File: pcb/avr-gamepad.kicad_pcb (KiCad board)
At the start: 2 copper layers, 53.1 x 53 mm, 57 parts, among them J1 Conn_01x06, J2 Conn_01x06, J3 Conn_01x05, J4 Conn_01x05, P1 USB_C_Plug_USB2.0, SW1 RESET, SW10 R2, SW11 A, SW13 Left, SW14 L2, SW16 B, SW17 Start, SW18 Y, SW19 X, SW2 Right, SW3 Up, SW4 Down, SW6 Select, SW7 L1, SW8 R1, U1 ATmega32U4-AU, U2 PCF8574, U3 PCF8574, Y1 Crystal_GND24

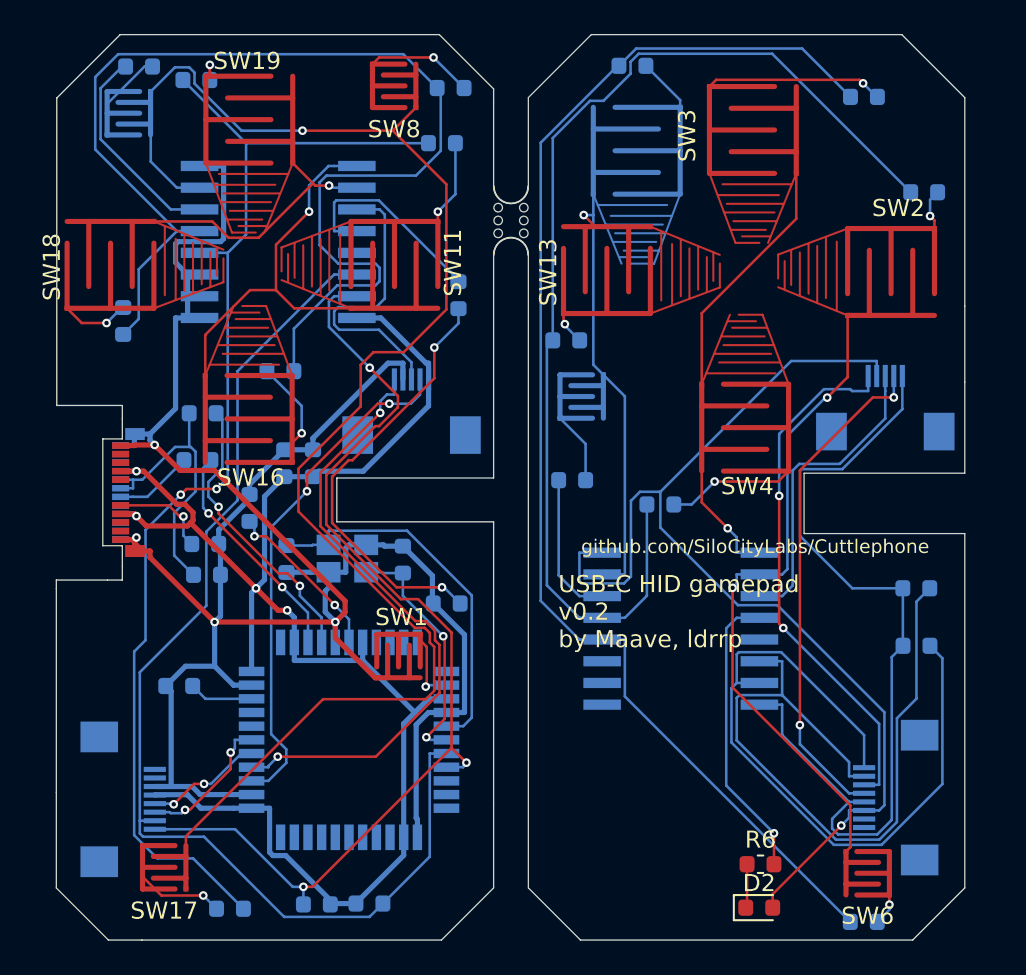
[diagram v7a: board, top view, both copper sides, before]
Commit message: pcb rearranging, placeholder footprint for right angle tact switches
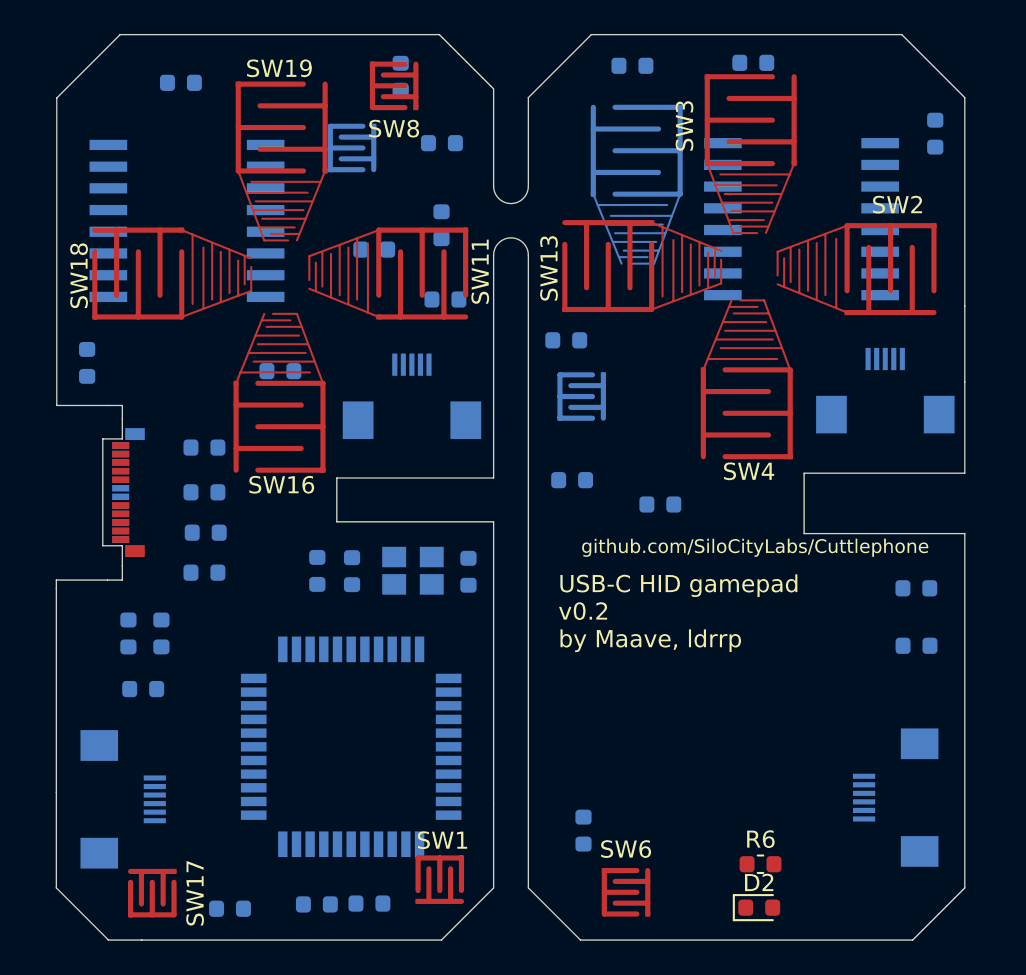
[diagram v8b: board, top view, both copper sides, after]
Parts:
- removed mouse-bite-2mm-slot: VAL**, Panelization:mouse-bite-2mm-slot
- J1, J2: footprint Connector_FFC-FPC:Hirose_FH12-8S-0.5SH_1x08-1MP_P0.50mm_Horizontal -> Connector_FFC-FPC:Hirose_FH12-6S-0.5SH_1x06-1MP_P0.50mm_Horizontal
- moved U2 25.0 mm to (171.0, 91.2)
- moved D1 17.8 mm to (150.2, 95.9)
- moved D13 17.4 mm to (146.0, 93.0), turned to 180 degrees
- moved D3 17.2 mm to (158.3, 126.9), turned to 270 degrees
- moved SW6 14.2 mm to (160.8, 130.6), turned to 0 degrees
- moved C1 13.5 mm to (131.7, 115.4)
- moved C2 13.3 mm to (133.6, 115.4)
- moved SW1 13.3 mm to (149.9, 129.8)
- moved SW10 13.2 mm to (144.8, 87.0)
- moved R4 7.44 mm to (136.1, 104.5)
- moved D8 6.77 mm to (168.2, 82.0)
- moved U3 5.47 mm to (135.1, 91.3)
- moved C6 5.41 mm to (142.7, 111.8)
- moved R1 4.62 mm to (136.1, 107.2)
- moved R2 4.27 mm to (136.2, 109.5)
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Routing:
- net GND: track 142.1 -> 0.00 mm, vias 4 -> 0
- net +5V: track 93.5 -> 0.00 mm, vias 4 -> 0
- net /Col1: track 89.6 -> 0.00 mm, vias 1 -> 0
- net /RowL1: track 76.2 -> 0.00 mm
- net /Row1: track 69.9 -> 0.00 mm, vias 2 -> 0
- net /Row2: track 69.8 -> 0.00 mm
- net /SCL: track 67.1 -> 0.00 mm
- net /RowL2: track 65.6 -> 0.00 mm
- net /GND_L: track 64.1 -> 0.00 mm, vias 1 -> 0
- net /SDA: track 60.7 -> 0.00 mm, vias 3 -> 0
- net /VCC_L: track 49.8 -> 0.00 mm
- net /SDA_L: track 42.7 -> 0.00 mm
- net /SCL_L: track 42.4 -> 0.00 mm
- net /ColL3: track 38.7 -> 0.00 mm, vias 2 -> 0
- net /JoyRightX: track 36.4 -> 0.00 mm, vias 2 -> 0
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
